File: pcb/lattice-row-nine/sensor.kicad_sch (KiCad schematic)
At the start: 3 parts, among them U5 LPS22HH

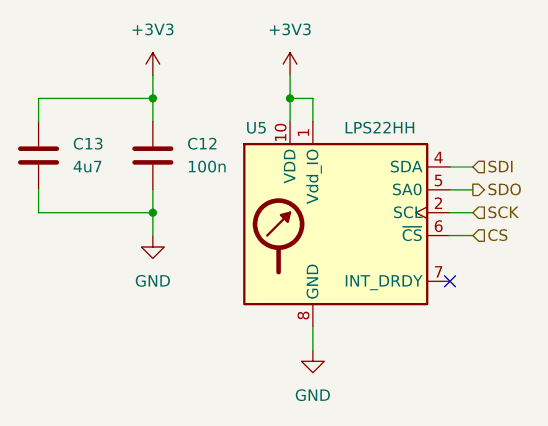
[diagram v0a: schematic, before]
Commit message: Add part numbers
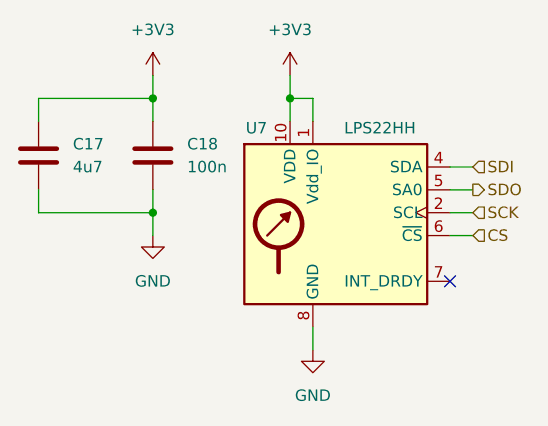
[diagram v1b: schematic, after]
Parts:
- renumbered C13 to C17, C12 to C18, U5 to U7
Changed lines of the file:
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@@
 		(dnp no)
 		(fields_autoplaced yes)
-		(property "Reference" "#PWR030"
+		(property "Reference" "#PWR038"
 			(at 99.06 80.01 0)
 			(effects
@@
 		(dnp no)
 		(fields_autoplaced yes)
-		(property "Reference" "#PWR028"
+		(property "Reference" "#PWR036"
 			(at 96.52 46.99 0)
 			(effects
@@
 		(on_board yes)
 		(dnp no)
-		(property "Reference" "U5"
+		(property "Reference" "U7"
 			(at 93.98 49.022 0)
 			(effects
@@
 		(dnp no)
 		(fields_autoplaced yes)
-		(property "Reference" "#PWR025"
+		(property "Reference" "#PWR037"
 			(at 81.28 67.31 0)
 			(effects
@@
 		(dnp no)
 		(fields_autoplaced yes)
-		(property "Reference" "#PWR023"
+		(property "Reference" "#PWR035"
 			(at 81.28 46.99 0)
 			(effects
@@
 		(dnp no)
 		(fields_autoplaced yes)
-		(property "Reference" "C13"
+		(property "Reference" "C17"
 			(at 72.39 50.7999 0)
 			(effects
@@
 		(dnp no)
 		(fields_autoplaced yes)
-		(property "Reference" "C12"
+		(property "Reference" "C18"
 			(at 85.09 50.7999 0)
 			(effects
